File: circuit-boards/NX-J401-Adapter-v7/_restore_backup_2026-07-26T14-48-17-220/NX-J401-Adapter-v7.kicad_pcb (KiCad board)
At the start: 4 copper layers, 120.3 x 79 mm, 135 parts, among them J1 Terminal, J10 POWER, J11 USB_C_Receptacle_USB2.0_14P, J2 Terminal, J3 NX CONTROL & UART, J4 15V, J5 NX CONTROL & UART, J6 NX CONTROL & UART, J7 USB1, J8 SWD, J9 CAN1, Q1 CSD19534Q5A, Q2 SI2301CDS-T1-GE3, Q3 CSD17578Q5A, Q4 CSD17578Q5A, Q5 SS8050, Q6 CSD19534Q5A, Q7 SI2301CDS-T1-GE3, Q8 CSD19534Q5A, Q9 CSD19534Q5A, SW1 RESET, SW2 RECOVERY, U1 LM74700QDBVRQ1, U2 TPS613222ADBV, U3 STM32G431CBTx, U5 ISO6721BDR, U6 FT232RNL, U7 LM74700QDBVRQ1, U8 TJA1051T/3/1J

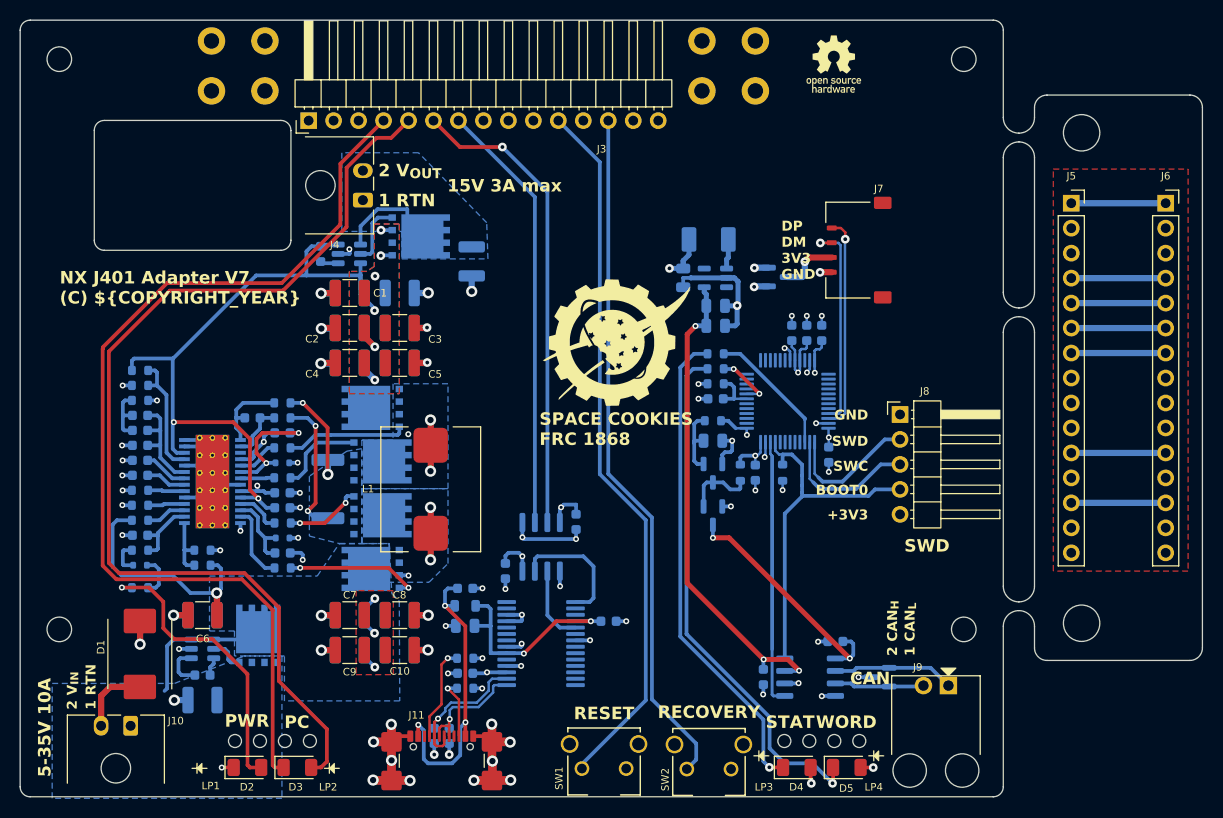
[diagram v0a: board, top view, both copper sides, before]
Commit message: Removed boot0 switch to clear J401 40 pin header
Signed-off-by: scott <scott@scott-Z590I-AORUS-ULTRA.bb>
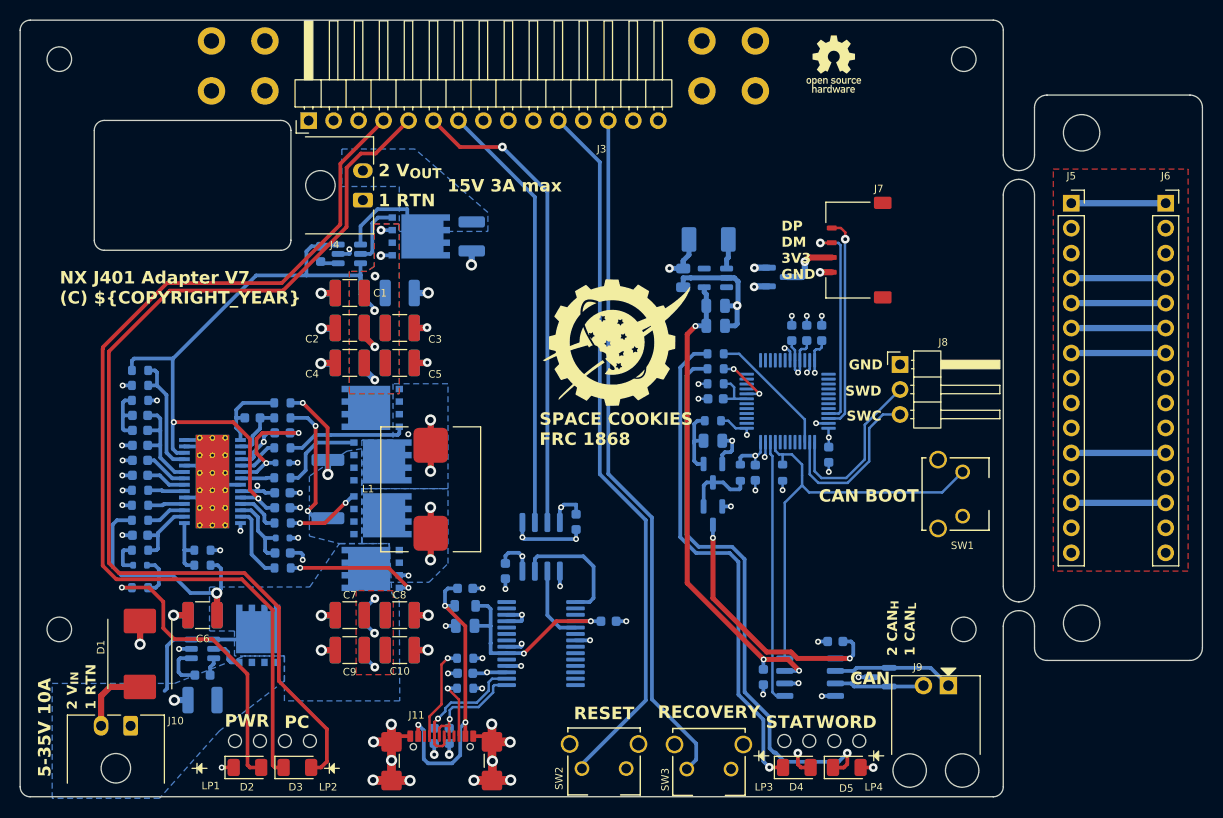
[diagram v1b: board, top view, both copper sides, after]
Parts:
- added SW1: CAN BOOT, NX-J401-Adapter:SW_TL1105VF100Q_EWI, F.Cu at (251.9, 125.0)
- J8: footprint NX-J401-Adapter:PinHeader_1x05_P2.54mm_Horizontal -> NX-J401-Adapter:PinHeader_1x03_P2.54mm_Horizontal
- moved J8 5.08 mm to (245.5, 109.6)
- moved C11 2.54 mm to (201.9, 96.5)
- renumbered C12 to C11, C11 to C12, SW1 to SW2, SW2 to SW3
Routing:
- net /CANable2.0/BOOT0: track 35.9 -> 43.1 mm
- net Net-(D5-K): track 53.4 -> 57.4 mm
- net /CANable2.0/SWDIO: track 14.0 -> 17.7 mm
- net /CANable2.0/3V3_CAN: track 24.6 -> 28.2 mm
- net /CANable2.0/SWCLK: track 14.4 -> 17.7 mm
- net Net-(D4-K): track 49.2 -> 51.2 mm
- net /CANable2.0/3V3: track 33.3 -> 34.2 mm
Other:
- outline, holes or cut-outs redrawn
- board text removed: "+3V3"
- board text removed: "BOOT0"
